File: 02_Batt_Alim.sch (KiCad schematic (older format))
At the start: 49 parts, among them IC1 TP4056, IC2 DW01A, J1 Conn_01x01, J10 Conn_01x01, J11 Conn_01x01, J12 Conn_01x01, J2 Conn_01x01, J3 Conn_01x01, J4 Conn_01x01, J5 Conn_01x01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

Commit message: dernières modification et routage avec plan de cuivre
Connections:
- net V_BAT+_F: now reaches C5.1, IC2.5 (VCC), R16.1
- net LX: now reaches D5.1 (K), L1.1, U1.2 (LX)
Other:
- note removed: "change symbol so that exposed pad is connected to ground"
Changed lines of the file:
@@
 Text GLabel 5000 3375 0    50   Input ~ 0
 V_ext_p
-Text Notes 1525 1775 0    50   ~ 0
-change symbol so that exposed pad is connected to ground
+Text Label 7800 3800 0    50   ~ 0
+LX
+Text Label 1900 5800 0    50   ~ 0
+V_BAT+_F
 $EndSCHEMATC

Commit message: corrected diodes schematics; gerbers generation
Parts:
- removed D1, D4, D5, D7: 1N5819W, Diode_SMD:D_SOD-123F, symbol pspice:DIODE
- added D1, D4, D5, D7, D8: 1N5819W, Diode_SMD:D_SOD-123F, symbol Device:D_ALT
- Q1, Q3: MANUFACTURER Alpha & Omega Semiconductor -> (none); MAXIMUM_PACKAGE_HEIGHT 1.75 mm -> (none); PARTREV I -> (none); STANDARD IPC 7351B -> (none)
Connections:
- net 5V: now also D5.1 (K)
- net LX: now also D5.2 (A)
- net SWITCH_IN: now also D4.1 (K)
- net SWITCH_OUT: now also D1.2 (A)
- net V_OUT: now also D1.1 (K)
- net V_ext: now also D7.2 (A), D8.2 (A)
- net V_ext_p: now also D4.2 (A), D7.1 (K), D8.1 (K)
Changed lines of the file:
@@
-	1    0    0    -1
-$EndComp
-$Comp
-L pspice:DIODE D?
-U 1 1 5FD40EA1
-P 5325 1525
-AR Path="/5FD39726/5FD40EA1" Ref="D?"  Part="1"
-AR Path="/5FD40EA1" Ref="D1"  Part="1"
-F 0 "D1" H 5325 1790 50  0000 C CNN
-F 1 "1N5819W" H 5325 1699 50  0000 C CNN
-F 2 "Diode_SMD:D_SOD-123F" H 5325 1525 50  0001 C CNN
-F 3 "C169540" H 5325 1525 50  0001 C CNN
-	1    5325 1525
 	1    0    0    -1
 $EndComp
@@
 Wire Wire Line
 	7850 2025 7850 2100
-Wire Wire Line
-	5050 1525 5125 1525
 Wire Wire Line
 	5050 2000 5075 2000
@@
 F 1 "AO4407A" V 5579 2100 50  0000 C CNN
 F 2 "Package_SO:SOIC-8_3.9x4.9mm_P1.27mm" H 5325 2100 50  0001 L BNN
-F 3 "" H 5325 2100 50  0001 L BNN
-F 4 "Alpha & Omega Semiconductor" H 5325 2100 50  0001 L BNN "MANUFACTURER"
-F 5 "1.75 mm" H 5325 2100 50  0001 L BNN "MAXIMUM_PACKAGE_HEIGHT"
-F 6 "I" H 5325 2100 50  0001 L BNN "PARTREV"
-F 7 "IPC 7351B" H 5325 2100 50  0001 L BNN "STANDARD"
+F 3 "C16072 " H 5325 2100 50  0001 L BNN
+F 4 "" H 5325 2100 50  0001 L BNN "MANUFACTURER"
+F 5 "" H 5325 2100 50  0001 L BNN "MAXIMUM_PACKAGE_HEIGHT"
+F 6 "" H 5325 2100 50  0001 L BNN "PARTREV"
+F 7 "" H 5325 2100 50  0001 L BNN "STANDARD"
 	1    5325 2100
 	0    -1   -1   0
@@
 F 1 "AO4407A" V 5604 3975 50  0000 C CNN
 F 2 "Package_SO:SOIC-8_3.9x4.9mm_P1.27mm" H 5350 3975 50  0001 L BNN
-F 3 "" H 5350 3975 50  0001 L BNN
-F 4 "Alpha & Omega Semiconductor" H 5350 3975 50  0001 L BNN "MANUFACTURER"
-F 5 "1.75 mm" H 5350 3975 50  0001 L BNN "MAXIMUM_PACKAGE_HEIGHT"
-F 6 "I" H 5350 3975 50  0001 L BNN "PARTREV"
-F 7 "IPC 7351B" H 5350 3975 50  0001 L BNN "STANDARD"
+F 3 "C16072 " H 5350 3975 50  0001 L BNN
+F 4 "" H 5350 3975 50  0001 L BNN "MANUFACTURER"
+F 5 "" H 5350 3975 50  0001 L BNN "MAXIMUM_PACKAGE_HEIGHT"
+F 6 "" H 5350 3975 50  0001 L BNN "PARTREV"
+F 7 "" H 5350 3975 50  0001 L BNN "STANDARD"
 	1    5350 3975
 	0    1    -1   0
-$EndComp
-$Comp
-L pspice:DIODE D?
-U 1 1 5FDE24D0
-P 5375 3375
-AR Path="/5FD39726/5FDE24D0" Ref="D?"  Part="1"
-AR Path="/5FDE24D0" Ref="D4"  Part="1"
-F 0 "D4" H 5375 3640 50  0000 C CNN
-F 1 "1N5819W" H 5375 3549 50  0000 C CNN
-F 2 "Diode_SMD:D_SOD-123F" H 5375 3375 50  0001 C CNN
-F 3 "C169540" H 5375 3375 50  0001 C CNN
-	1    5375 3375
-	1    0    0    -1
 $EndComp
 $Comp
@@
 $EndComp
 Wire Wire Line
-	5000 3375 5175 3375
-Wire Wire Line
-	5575 3375 5650 3375
-Wire Wire Line
 	5075 3875 5150 3875
 Wire Wire Line
@@
 	0    1    1    0
 $EndComp
-$Comp
-L pspice:DIODE D?
-U 1 1 5FE07378
-P 8125 3500
-AR Path="/5FD39726/5FE07378" Ref="D?"  Part="1"
-AR Path="/5FE07378" Ref="D5"  Part="1"
-F 0 "D5" H 8125 3765 50  0000 C CNN
-F 1 "1N5819W" H 8125 3674 50  0000 C CNN
-F 2 "Diode_SMD:D_SOD-123F" H 8125 3500 50  0001 C CNN
-F 3 "C169540" H 8125 3500 50  0001 C CNN
-	1    8125 3500
-	1    0    0    -1
-$EndComp
 Wire Wire Line
 	7225 3650 7225 3500
@@
 	7700 3500 7800 3500
 Connection ~ 7800 3500
-Wire Wire Line
-	7800 3500 7925 3500
 Wire Wire Line
 	8400 4375 8475 4375
@@
 Connection ~ 2300 3900
 Wire Wire Line
-	2300 3900 2300 3775
-Wire Wire Line
 	2325 4250 2300 4250
 Connection ~ 2300 4250
@@
 	8900 5950 11250 5950
 Wire Wire Line
-	1325 3550 1400 3550
-$Comp
-L pspice:DIODE D?
-U 1 1 5FEAFA8C
-P 1600 3550
-AR Path="/5FD39726/5FEAFA8C" Ref="D?"  Part="1"
-AR Path="/5FEAFA8C" Ref="D7"  Part="1"
-F 0 "D7" H 1600 3815 50  0000 C CNN
-F 1 "1N5819W" H 1600 3724 50  0000 C CNN
-F 2 "Diode_SMD:D_SOD-123F" H 1600 3550 50  0001 C CNN
-F 3 "C169540" H 1600 3550 50  0001 C CNN
-	1    1600 3550
-	1    0    0    -1
-$EndComp
-Wire Wire Line
 	1800 3550 2300 3550
-Text GLabel 2050 3775 0    50   Input ~ 0
+Text GLabel 2025 4575 0    50   Input ~ 0
 V_ext_p
-Wire Wire Line
-	2050 3775 2300 3775
-Connection ~ 2300 3775
-Wire Wire Line
-	2300 3775 2300 3550
 Text GLabel 4950 4175 0    50   Input ~ 0
 V_ext_p
@@
 Text Label 1900 5800 0    50   ~ 0
 V_BAT+_F
+$Comp
+L Device:D_ALT D4
+U 1 1 5FDA974E
+P 5375 3375
+F 0 "D4" H 5375 3158 50  0000 C CNN
+F 1 "1N5819W" H 5375 3249 50  0000 C CNN
+F 2 "Diode_SMD:D_SOD-123F" H 5375 3375 50  0001 C CNN
+F 3 "C369930" H 5375 3375 50  0001 C CNN
+	1    5375 3375
+	-1   0    0    1
+$EndComp
+Wire Wire Line
+	5525 3375 5650 3375
+Wire Wire Line
+	5000 3375 5225 3375
+$Comp
+L Device:D_ALT D7
+U 1 1 5FDB60BA
+P 1650 3550
+F 0 "D7" H 1650 3333 50  0000 C CNN
+F 1 "1N5819W" H 1650 3424 50  0000 C CNN
+F 2 "Diode_SMD:D_SOD-123F" H 1650 3550 50  0001 C CNN
+F 3 "C369930" H 1650 3550 50  0001 C CNN
+	1    1650 3550
+	-1   0    0    1
+$EndComp
+$Comp
+L Device:D_ALT D8
+U 1 1 5FDB69C2
+P 1650 3900
+F 0 "D8" H 1650 3683 50  0000 C CNN
+F 1 "1N5819W" H 1650 3774 50  0000 C CNN
+F 2 "Diode_SMD:D_SOD-123F" H 1650 3900 50  0001 C CNN
+F 3 "C369930" H 1650 3900 50  0001 C CNN
+	1    1650 3900
+	-1   0    0    1
+$EndComp
+Wire Wire Line
+	1325 3550 1375 3550
+Wire Wire Line
+	2025 4575 2300 4575
+Connection ~ 2300 4575
+Wire Wire Line
+	1500 3900 1375 3900
+Wire Wire Line
+	1375 3900 1375 3550
+Connection ~ 1375 3550
+Wire Wire Line
+	1375 3550 1500 3550
+Wire Wire Line
+	1800 3900 2300 3900
+Wire Wire Line
+	2300 3550 2300 3900
+$Comp
+L Device:D_ALT D1
+U 1 1 5FDCC581
+P 5375 1525
+F 0 "D1" H 5375 1308 50  0000 C CNN
+F 1 "1N5819W" H 5375 1399 50  0000 C CNN
+F 2 "Diode_SMD:D_SOD-123F" H 5375 1525 50  0001 C CNN
+F 3 "C369930" H 5375 1525 50  0001 C CNN
+	1    5375 1525
+	-1   0    0    1
+$EndComp
+Wire Wire Line
+	5050 1525 5225 1525
+$Comp
+L Device:D_ALT D5
+U 1 1 5FDD39F1
+P 8175 3500
+F 0 "D5" H 8175 3283 50  0000 C CNN
+F 1 "1N5819W" H 8175 3374 50  0000 C CNN
+F 2 "Diode_SMD:D_SOD-123F" H 8175 3500 50  0001 C CNN
+F 3 "C369930" H 8175 3500 50  0001 C CNN
+	1    8175 3500
+	-1   0    0    1
+$EndComp
+Wire Wire Line
+	7800 3500 8025 3500
 $EndSCHEMATC

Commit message: simplify!
1) battery lipo protection deleted
2) move to schottky diodes instead of pmos for avoiding perturbation of charge while switch is on.
3) reduced size of pcb
4) added nmos for "hold" function
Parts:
- removed C5: 100nF, Capacitor_SMD:C_0603_1608Metric, symbol Device:C
- removed IC2: DW01A, Chimere:SOT23-6, symbol Chimere:DW01A
- removed Q3: AO4407A, Package_SO:SOIC-8_3.9x4.9mm_P1.27mm, symbol Chimere:AO4407A
- removed Q4: FS8205A, Chimere:SOP65P640X120-8N, symbol Chimere:FS8205A
- removed R16: 100, Resistor_SMD:R_0603_1608Metric, symbol Device:R
- removed R17: 1k, Resistor_SMD:R_0603_1608Metric, symbol Device:R
- added Q3: 2N7002, Package_TO_SOT_SMD:SOT-23, symbol Transistor_FET:2N7002
- R11: value 100 -> 100K
- R13: value 100K -> 100
- R7: value 1k2 -> 10k
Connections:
- net V_BAT- is gone; now on net GND: J10.1 (Pin_1)
- net GND: now also R11.2, Q3.2 (S); no longer R13.2
- net SWITCH_IN: now also D8.1 (K)
- net V_BAT+: now also D8.2 (A)
- net V_ext: now also D4.2 (A); no longer D8.2 (A)
- net V_ext_p: no longer D4.2 (A), D8.1 (K), R11.1, R13.1
- net uC_2_V: now also R11.1, R13.1; no longer R3.2, R4.1
- new net: Q3.3 (D), R3.2, R4.1
- new net: Q3.1 (G), R13.2
- no-connect marks 2 -> 0
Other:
- note added: "Battery is Olimex \nBATTERY-LIPO250mAh\n"
- note added: "charge à 130mA"
- note added: "uC_2_V :\n1: maintien\n0: arrêt"
- note removed: "Battery is NCR18650B\nLi-Ion MH12210"
- note removed: "battery protection"
- note removed: "uC_2_V :\n0: maintien\n1: arrêt"
- moved on the sheet: D8, Q2, R1, R2, R5

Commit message: simplification
simplified the whole design
Gerbers generated
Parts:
- removed D1: 1N5819W, Diode_SMD:D_SOD-123F, symbol Device:D_ALT
- removed J10, J11, J12, J4, J5, J6, J7, J8: Conn_01x01, Chimere:Castellated_conn, symbol Connector_Generic:Conn_01x01
- removed Q1: AO4407A, Package_SO:SOIC-8_3.9x4.9mm_P1.27mm, symbol Chimere:AO4407A
- removed Q2, Q3: 2N7002, Package_TO_SOT_SMD:SOT-23, symbol Transistor_FET:2N7002
- removed R1, R11, R3, R5: 100K, Resistor_SMD:R_0603_1608Metric, symbol Device:R
- removed R13, R2, R4: 100, Resistor_SMD:R_0603_1608Metric, symbol Device:R
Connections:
- net V_OUT is gone; now on net V_sum: C4.1, L1.2
- net SWITCH_IN renamed V_sum
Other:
- note added: "Battery"
- note removed: "CONTROL"
- note removed: "Graceful switch"
- note removed: "Power On/Off\n switch"
- note removed: "V_2_uC\nétat de l'interrupteur:\n0 : passant ON\n1 : ouvert OFF\n"
- note removed: "nmos"
- note removed: "pmos:\nPackage_SO:SOIC-8_3.9x4.9mm_P1.27mm\nC16072\n"
- note removed: "tension \navant DC/DC"
- note removed: "uC_2_V :\n1: maintien\n0: arrêt"
- moved on the sheet: J9

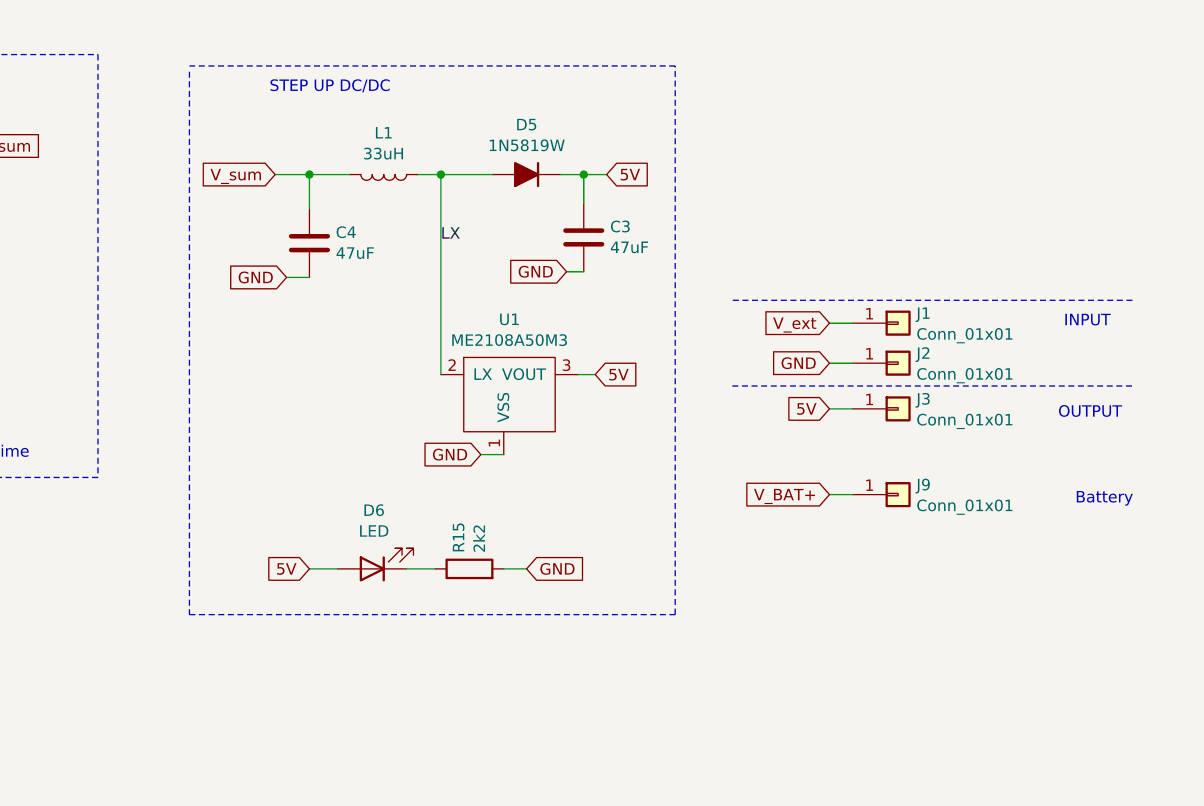
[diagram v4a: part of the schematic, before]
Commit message: coupé en deux
séparé la partie dcdc du chargeur;
schéma fait et routage en cours de modification
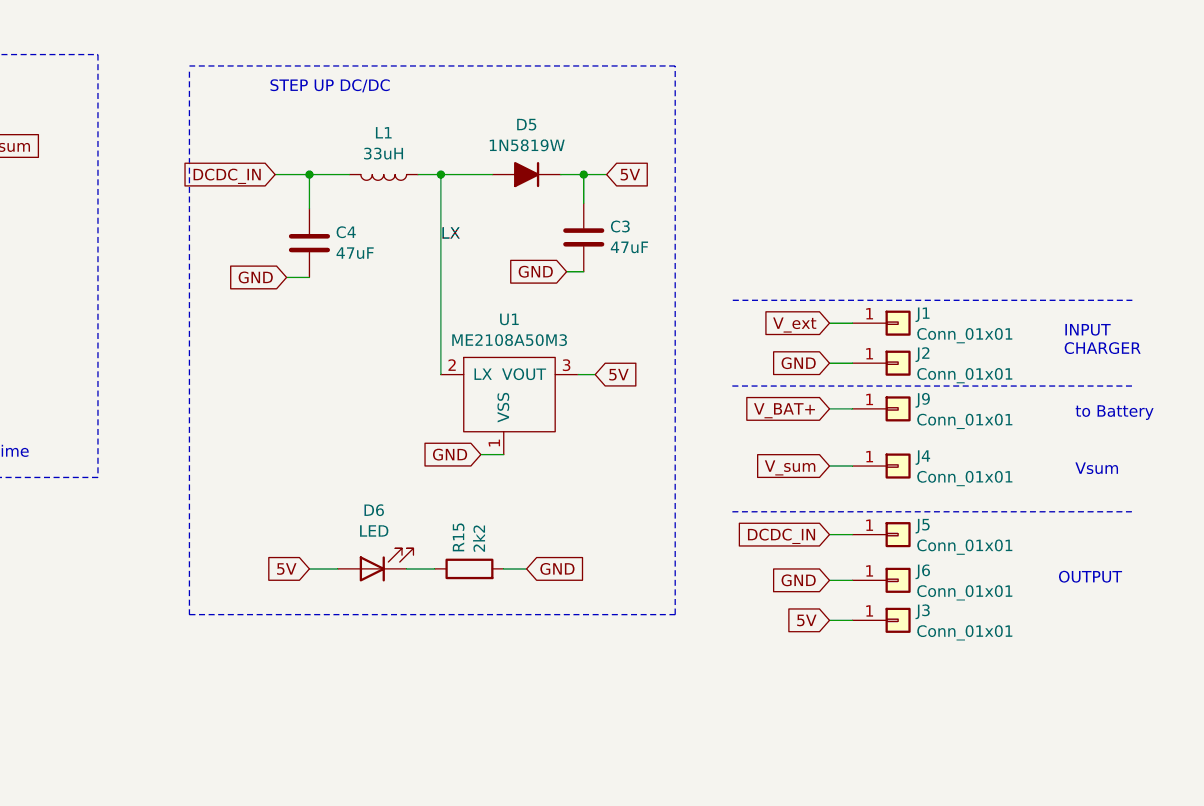
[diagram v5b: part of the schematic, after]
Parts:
- added J4, J5, J6: Conn_01x01, Chimere:Castellated_conn, symbol Connector_Generic:Conn_01x01
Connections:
- net GND: now also J6.1 (Pin_1)
- net V_sum: now also J4.1 (Pin_1); no longer C4.1, L1.2
- new net DCDC_IN: C4.1, J5.1 (Pin_1), L1.2
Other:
- note added: "INPUT\nCHARGER"
- note added: "Vsum"
- note added: "to Battery"
- note removed: "Battery"
- note removed: "INPUT"
- moved on the sheet: J3, J9
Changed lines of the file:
@@
 Text GLabel 5725 3375 2    50   Input ~ 0
 V_sum
-Text GLabel 9500 4525 0    50   Input ~ 0
+Text GLabel 9500 5450 0    50   Input ~ 0
 5V
 $Comp
@@
 L Connector_Generic:Conn_01x01 J3
 U 1 1 5FDA56A3
-P 9800 4525
-F 0 "J3" H 9880 4567 50  0000 L CNN
-F 1 "Conn_01x01" H 9880 4476 50  0000 L CNN
-F 2 "Chimere:Castellated_conn" H 9800 4525 50  0001 C CNN
-F 3 "~" H 9800 4525 50  0001 C CNN
-	1    9800 4525
-	1    0    0    -1
-$EndComp
-Wire Wire Line
-	9500 4525 9600 4525
-Text Notes 10525 4175 0    50   ~ 0
-INPUT
-Text Notes 10500 4575 0    50   ~ 0
+P 9800 5450
+F 0 "J3" H 9880 5492 50  0000 L CNN
+F 1 "Conn_01x01" H 9880 5401 50  0000 L CNN
+F 2 "Chimere:Castellated_conn" H 9800 5450 50  0001 C CNN
+F 3 "~" H 9800 5450 50  0001 C CNN
+	1    9800 5450
+	1    0    0    -1
+$EndComp
+Wire Wire Line
+	9500 5450 9600 5450
+Text Notes 10525 4300 0    50   ~ 0
+INPUT\nCHARGER
+Text Notes 10500 5300 0    50   ~ 0
 OUTPUT
 Wire Notes Line
@@
 Text Label 1875 3550 0    50   ~ 0
 V_ext_p
-Text GLabel 7075 3500 0    50   Input ~ 0
-V_sum
 $Comp
 L Connector_Generic:Conn_01x01 J9
 U 1 1 5FE2AEFB
-P 9800 4900
-F 0 "J9" H 9880 4942 50  0000 L CNN
-F 1 "Conn_01x01" H 9880 4851 50  0000 L CNN
-F 2 "Chimere:Castellated_conn" H 9800 4900 50  0001 C CNN
-F 3 "~" H 9800 4900 50  0001 C CNN
-	1    9800 4900
-	1    0    0    -1
-$EndComp
-Wire Wire Line
-	9500 4900 9600 4900
-Text GLabel 9500 4900 0    50   Input ~ 0
+P 9800 4525
+F 0 "J9" H 9880 4567 50  0000 L CNN
+F 1 "Conn_01x01" H 9880 4476 50  0000 L CNN
+F 2 "Chimere:Castellated_conn" H 9800 4525 50  0001 C CNN
+F 3 "~" H 9800 4525 50  0001 C CNN
+	1    9800 4525
+	1    0    0    -1
+$EndComp
+Wire Wire Line
+	9500 4525 9600 4525
+Text GLabel 9500 4525 0    50   Input ~ 0
 V_BAT+
-Text Notes 10575 4950 0    50   ~ 0
-Battery
+Text Notes 10575 4575 0    50   ~ 0
+to Battery
 $Comp
 L Graphic:Logo_Open_Hardware_Small #LOGO1
@@
 	1    0    0    -1
 $EndComp
+Text GLabel 9500 5275 0    50   Input ~ 0
+GND
+$Comp
+L Connector_Generic:Conn_01x01 J6
+U 1 1 60A7F15C
+P 9800 5275
+F 0 "J6" H 9880 5317 50  0000 L CNN
+F 1 "Conn_01x01" H 9880 5226 50  0000 L CNN
+F 2 "Chimere:Castellated_conn" H 9800 5275 50  0001 C CNN
+F 3 "~" H 9800 5275 50  0001 C CNN
+	1    9800 5275
+	1    0    0    -1
+$EndComp
+Wire Wire Line
+	9500 5275 9600 5275
+Wire Notes Line
+	9075 4975 10825 4975
+$Comp
+L Connector_Generic:Conn_01x01 J5
+U 1 1 60A8BE36
+P 9800 5075
+F 0 "J5" H 9880 5117 50  0000 L CNN
+F 1 "Conn_01x01" H 9880 5026 50  0000 L CNN
+F 2 "Chimere:Castellated_conn" H 9800 5075 50  0001 C CNN
+F 3 "~" H 9800 5075 50  0001 C CNN
+	1    9800 5075
+	1    0    0    -1
+$EndComp
+Wire Wire Line
+	9500 5075 9600 5075
+Text GLabel 9500 5075 0    50   Input ~ 0
+DCDC_IN
+Text Notes 10575 4825 0    50   ~ 0
+Vsum
+$Comp
+L Connector_Generic:Conn_01x01 J4
+U 1 1 60A9782F
+P 9800 4775
+F 0 "J4" H 9880 4817 50  0000 L CNN
+F 1 "Conn_01x01" H 9880 4726 50  0000 L CNN
+F 2 "Chimere:Castellated_conn" H 9800 4775 50  0001 C CNN
+F 3 "~" H 9800 4775 50  0001 C CNN
+	1    9800 4775
+	1    0    0    -1
+$EndComp
+Wire Wire Line
+	9500 4775 9600 4775
+Text GLabel 9500 4775 0    50   Input ~ 0
+V_sum
+Text GLabel 7075 3500 0    50   Input ~ 0
+DCDC_IN
 $EndSCHEMATC

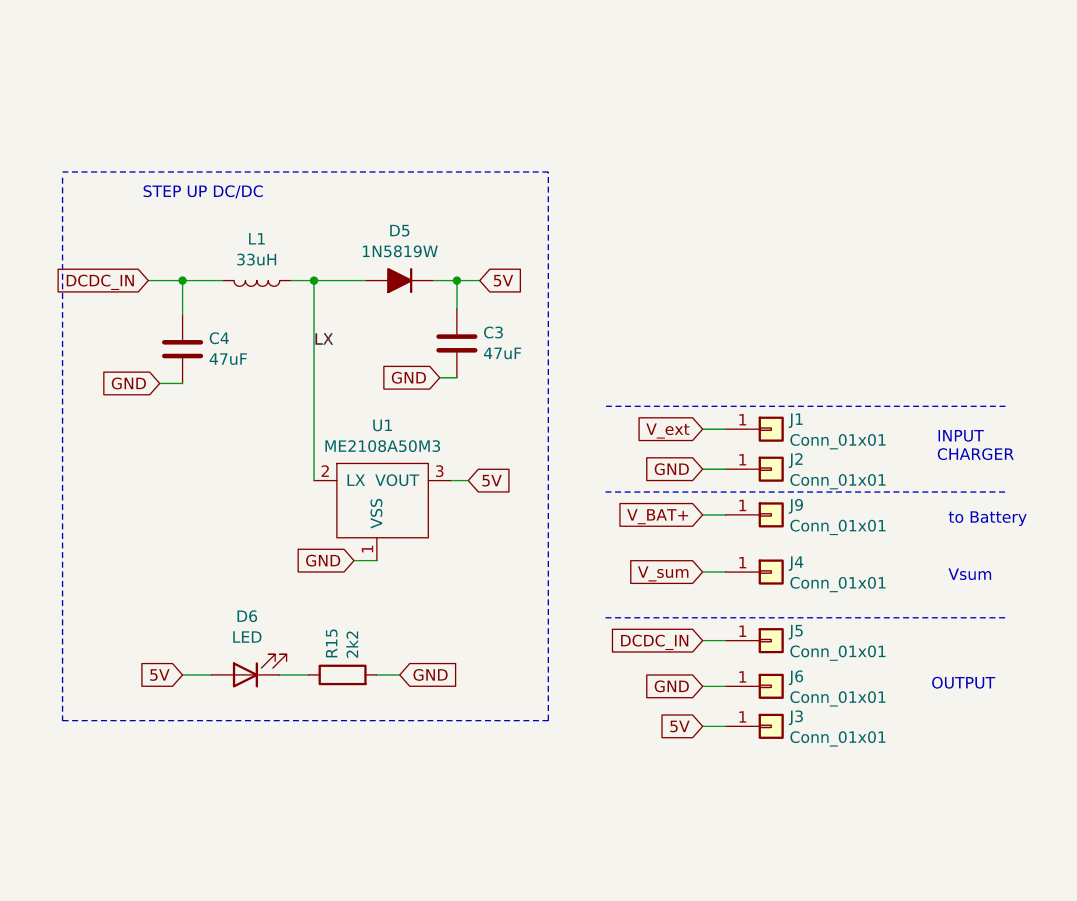
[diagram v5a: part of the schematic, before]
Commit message: modifications
ajout diode + capa pour filtrer + protection en sortie
changement inductance
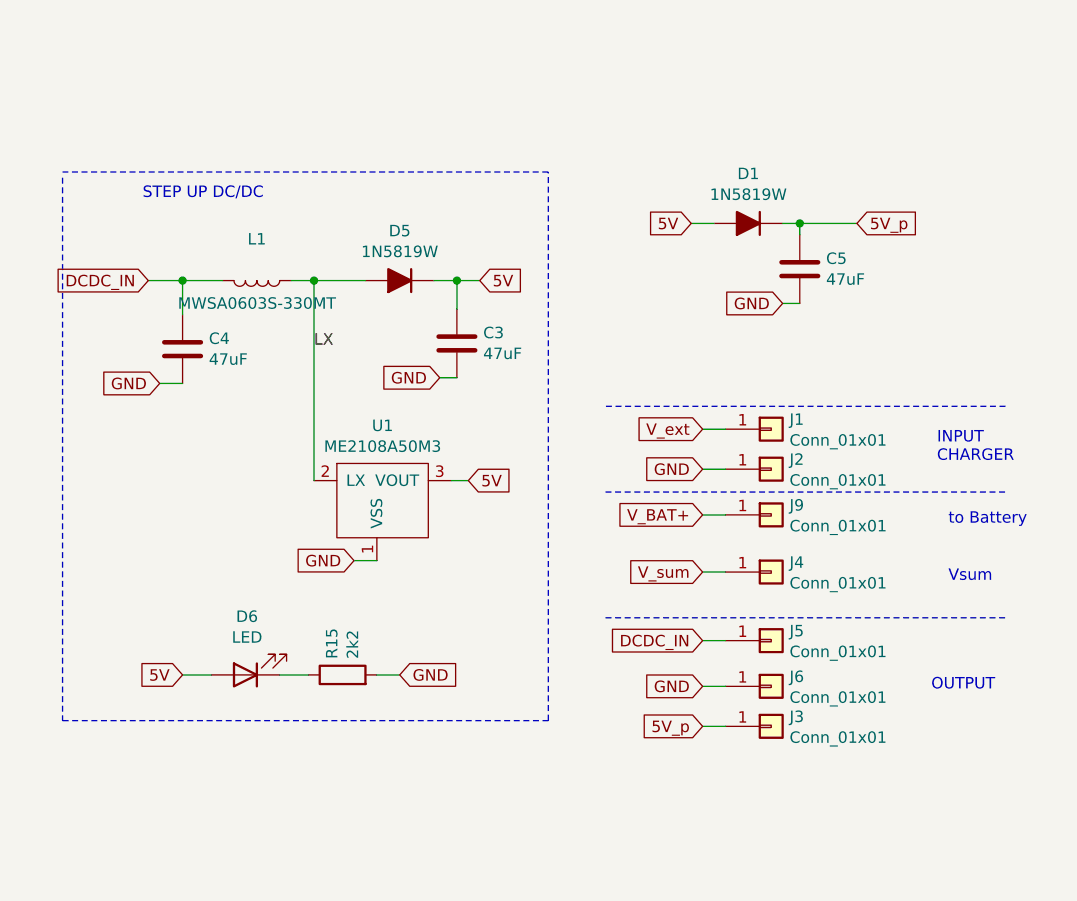
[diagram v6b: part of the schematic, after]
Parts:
- added C5: 47uF, Capacitor_SMD:C_1210_3225Metric, symbol Device:C
- added D1: 1N5819W, Diode_SMD:D_SOD-123F, symbol Device:D_ALT
- L1: value 33uH -> MWSA0603S-330MT; footprint Inductor_SMD:L_10.4x10.4_H4.8 -> Chimere:L_Sunlord_MWSA0603S_6.6x7.0x2.8mm
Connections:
- net 5V: now also D1.2 (A); no longer J3.1 (Pin_1)
- net GND: now also C5.2
- new net 5V_p: C5.1, D1.1 (K), J3.1 (Pin_1)
